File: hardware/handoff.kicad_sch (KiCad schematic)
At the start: 39 parts, among them J1 BAT JST-XH 2p, J2 PAD JST-XH 2p, J3 LED JST-XH 4p / 5mm RGB, J4 EXP 1x10, SW1 SS-12F23G5, U1 Raspberry Pi Pico 2 W, U2 MCP6292-E/MS

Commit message: Draw the SS-12F23G5 footprint and settle C4's pitch
SW1 gets a project footprint in hardware/handoff.pretty taken from the
vendor drawing: three 0.8 x 0.45 mm terminals at 3.0 mm pitch, two mounting
ears 12.9 mm overall, body 8.7 x 5.5 mm standing 3.3 mm behind the pin row.
Loads cleanly and passes DRC on a throwaway board. C4 is a 5 mm can on the
stock 2.5 mm-pitch footprint, per the owner.

Co-Authored-By: Claude Opus 5 <noreply@anthropic.com>
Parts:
- C4: footprint Capacitor_THT:CP_Radial_D5.0mm_P2.00mm -> Capacitor_THT:CP_Radial_D5.0mm_P2.50mm
- SW1: footprint Button_Switch_THT:SW_Slide_SPDT_Angled_CK_OS102011MA1Q -> handoff:SW_Slide_SS-12F23G5

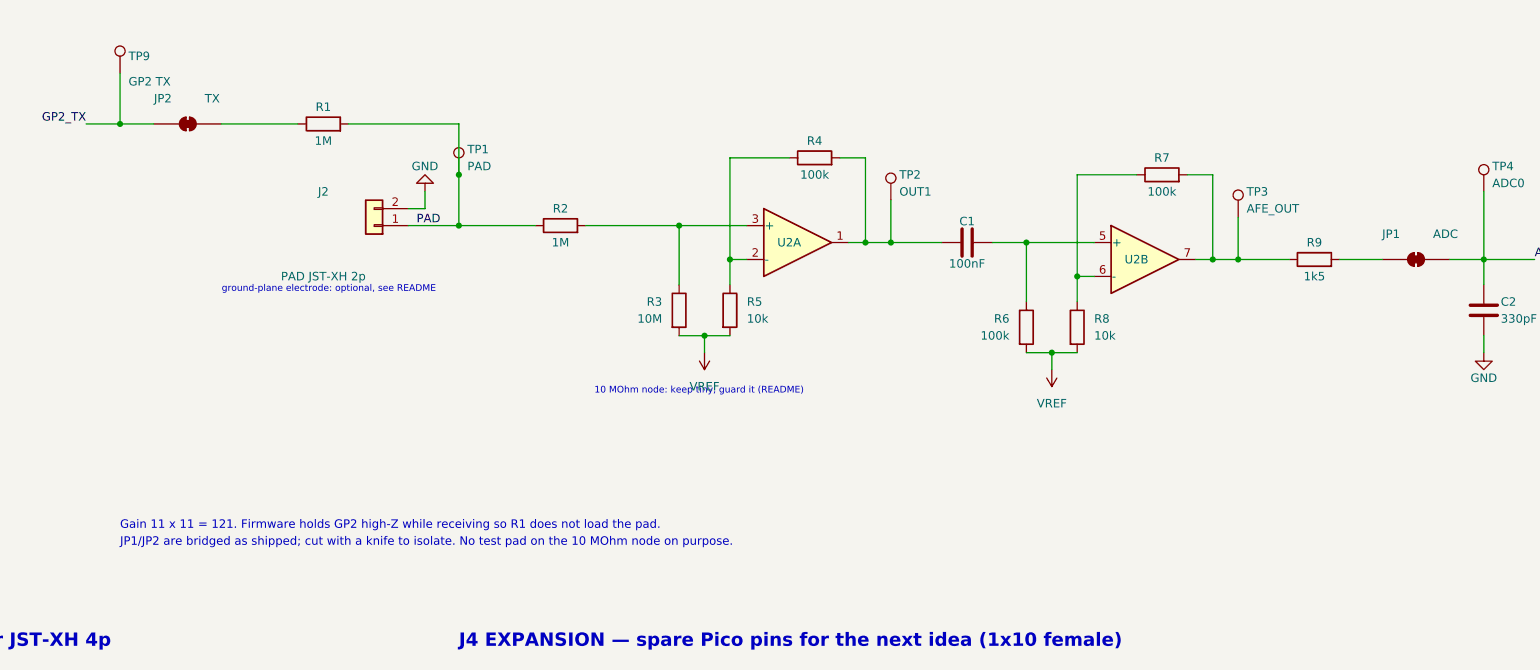
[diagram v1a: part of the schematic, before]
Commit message: Make every solder jumper normally open
Bridge with a blob to connect, wick to isolate; nothing is cut. Owner's
call: a blob is reversible, a knife cut is not. The board is inert as
delivered until JP1 and JP2 are bridged, which the README and the sheet
note now say. The review brief for the next session carries the same rule
into the jumpers it will add.

Co-Authored-By: Claude Opus 5 <noreply@anthropic.com>
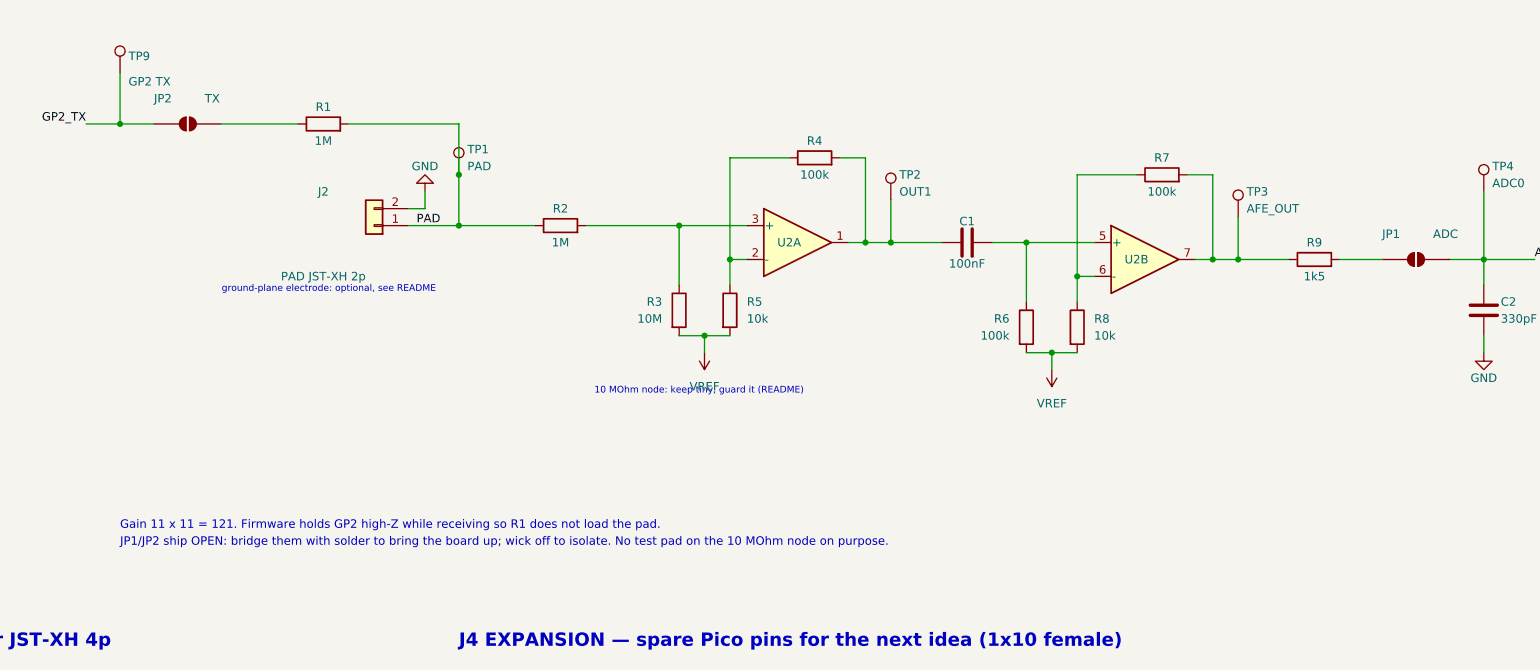
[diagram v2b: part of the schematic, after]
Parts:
- removed JP1: ADC, Jumper:SolderJumper-2_P1.3mm_Bridged_RoundedPad1.0x1.5mm, symbol Jumper:SolderJumper_2_Bridged
- removed JP2: TX, Jumper:SolderJumper-2_P1.3mm_Bridged_RoundedPad1.0x1.5mm, symbol Jumper:SolderJumper_2_Bridged
- added JP1: ADC, Jumper:SolderJumper-2_P1.3mm_Open_RoundedPad1.0x1.5mm, symbol Jumper:SolderJumper_2_Open
- added JP2: TX, Jumper:SolderJumper-2_P1.3mm_Open_RoundedPad1.0x1.5mm, symbol Jumper:SolderJumper_2_Open
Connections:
- net ADC0: now also JP1.2 (B)
- net GP2_TX: now also JP2.1 (A)
- net at R1.1: now also JP2.2 (B)
- net at R9.2: now also JP1.1 (A)
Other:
- note added: "JP1/JP2 ship OPEN: bridge them with solder to bring the board up; wick off to isolate. No test pad on the 10 MOhm node on purpose."
- note removed: "JP1/JP2 are bridged as shipped; cut with a knife to isolate. No test pad on the 10 MOhm node on purpose."

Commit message: Review the schematic before layout, and act on it
Pre-layout review of the untested PCBWay board. Report in hardware/review.md;
the generator is now the schematic's source and proves itself three ways
(ERC, EXPECTED_NETS pin for pin, BOM against the README parts table).

Wiring: all correct. U2 units map to the MCP6292 pinout, all 40 Pico pins
match, D1 and J1 polarity right, chain matches design section 7. 56 footprints
cross-checked pad-for-pad against their symbols with pcbnew. The brief's
"42 pads vs 40 pins" on the Pico footprint was a grep artefact: the two extra
hits are (pads not_allowed)/(pads allowed) inside its antenna keep-out rule.

Circuit, two real problems, both now measurable on the bench:

- GP2 leakage through R3 (10 MOhm) sets stage 1's DC point. 15 nA uses the
  whole headroom; RP2350-E9 can source 46 nA and park OUT1 on the rail. The
  owner's Pico 2 W is an A2, so E9 is live. Firmware must disable GP2's input
  buffer when high-Z; C6 (DNP, across JP2) AC-couples TX as the way out.
- Recovery after the board's own shout is ~3.6 ms on a body against the 1 ms
  budget, plus up to 13 ms through C1/R6 if the OOK-off chips drive GP2 low.
  Mains hum clips stage 2 at 13 mV on the 10 MOhm node.

Recommended but NOT applied, both value-only swaps on existing pads using
parts on hand, so the owner decides at M7: R3 10M -> 1M, C1 100n -> 330p.

Added, pads only unless noted: SW2 + R15 on GP15 (net BTN, the part the owner
chose), H1-H4 M3 mounting holes, J5 charger port in parallel with J1 (needs
one more 2-pin XH header), C5 bulk on U2's rail, C6 (DNP), JP3 3-way stage
select, JP4/JP5/JP6/JP7 in-line isolation, JP8 role strap on GP14, and
TP10-TP13. Every jumper ships open, so each is two nets in the oracle; the
README carries the jumper table and the bring-up order.

Also corrects the SS-12F23G5 footprint, which had the body standing 3.3 mm
behind the pin row with the handle vertical. Measured on the real part: it is
a right-angle switch lying flat on t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
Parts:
- added C5: 10uF 63V, Capacitor_THT:CP_Radial_D5.0mm_P2.50mm, symbol Device:C_Polarized
- added C6: 330pF C0G (DNP), Capacitor_SMD:C_1206_3216Metric_Pad1.33x1.80mm_HandSolder, symbol Device:C
- added H1, H2, H3, H4: M3, MountingHole:MountingHole_3.2mm_M3, symbol Mechanical:MountingHole
- added J5: CHG XH-2, Connector_JST:JST_XH_B2B-XH-A_1x02_P2.50mm_Vertical, symbol Connector_Generic:Conn_01x02
- added JP3: STAGE, Jumper:SolderJumper-3_P1.3mm_Open_RoundedPad1.0x1.5mm, symbol Jumper:SolderJumper_3_Open
- added JP4: U2 VDD, Jumper:SolderJumper-2_P1.3mm_Open_RoundedPad1.0x1.5mm, symbol Jumper:SolderJumper_2_Open
- added JP5: VSYS, Jumper:SolderJumper-2_P1.3mm_Open_RoundedPad1.0x1.5mm, symbol Jumper:SolderJumper_2_Open
- added JP6: VREF, Jumper:SolderJumper-2_P1.3mm_Open_RoundedPad1.0x1.5mm, symbol Jumper:SolderJumper_2_Open
- added JP7: RX, Jumper:SolderJumper-2_P1.3mm_Open_RoundedPad1.0x1.5mm, symbol Jumper:SolderJumper_2_Open
- added JP8: ROLE, Jumper:SolderJumper-2_P1.3mm_Open_RoundedPad1.0x1.5mm, symbol Jumper:SolderJumper_2_Open
- added R15: 10k, Resistor_SMD:R_1206_3216Metric_Pad1.30x1.75mm_HandSolder, symbol Device:R
- added SW2: TACT 6x6, Button_Switch_THT:SW_PUSH_6mm, symbol Switch:SW_Push
- added TP10: BAT+, TestPoint:TestPoint_Pad_D1.5mm, symbol Connector:TestPoint
- added TP11: D1_K, TestPoint:TestPoint_Pad_D1.5mm, symbol Connector:TestPoint
- added TP12: RX_IN, TestPoint:TestPoint_Pad_D1.5mm, symbol Connector:TestPoint
- added TP13: GND, TestPoint:TestPoint_Pad_D1.5mm, symbol Connector:TestPoint
- J1: value BAT JST-XH 2p -> BAT XH-2
- TP6: value 3V3 -> AFE_3V3
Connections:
- net +3V3: now also JP4.1 (A), R15.1; no longer C3.1, R10.1, TP6.1, U2.8 (V+)
- net BAT+: now also J5.2 (Pin_2), TP10.1
- net GND: now also C5.2, J5.1 (Pin_1), JP8.2 (B), SW2.2, TP13.1
- net GP2_TX: now also C6.1
- net PAD: now also JP7.1 (A); no longer R2.1
- net VREF: now also JP6.2 (B); no longer C4.1, R10.2, R11.1
- net VSYS: now also JP5.2 (B); no longer D1.1 (K)
- net at R7.2, TP3.1, U2.7: now also JP3.3 (B); no longer R9.1
- net OUT1: now reaches C1.1, R4.2, TP2.1, U2.1
- net OUT1: now also JP3.1 (A)
- net at JP2.2 (B), R1.1: now also C6.2
- net ROLE: now reaches U1.19 (GPIO14)
- net ROLE: now also JP8.1 (A)
- net BTN: now reaches U1.20 (GPIO15)
- net BTN: now also R15.2, SW2.1
- new net: D1.1 (K), JP5.1 (A), TP11.1
- new net: JP3.2 (C), R9.1
- new net: C4.1, JP6.1 (A), R10.2, R11.1
- new net: JP7.2 (B), R2.1, TP12.1
- new net AFE_3V3: C3.1, C5.1, JP4.2 (B), R10.1, TP6.1, U2.8 (V+)
- no-connect marks 18 -> 16
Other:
- note added: "BUTTON (GP15), ROLE strap (GP14), MOUNTING"
- note added: "Every JP ships OPEN: bridge with solder to bring the board up one stage at a time (README order); wick off to isolate. No test pad on the 10 MOhm node on purpose."
- note added: "Gain 11 x 11 = 121. Firmware holds GP2 high-Z with its input buffer OFF while receiving (RP2350-E9), so R1 does not load or bias the pad."
- note added: "H1-H4: 3.2 mm unplated, one per corner, not tied to GND"
- note added: "JP3: centre -> R9. Blob to pin 3 = stage 2 (x121); move it to pin 1 = stage 1 only (x11) if stage 2 clips. C6 is DNP: fit it instead of bridging JP2 to AC-couple TX."
- note added: "JP5 ships OPEN: bridge it to run from the cell (USB works regardless); open, TP11 -> TP8 is the ammeter position."
- note added: "U2 supply — AFE_3V3 behind JP4 (design §6.4 decoupling + C5 bulk)"
- note added: "VBUS (USB) and VSYS are OR'd inside the Pico; D1 stops VSYS back-feeding the cell and makes a reversed J1 harmless."
- note added: "no debounce cap: debounce in firmware"
- note added: "~0.35 V drop: VSYS 2.6-3.8 V, Pico needs 1.8-5.5 V. J5 is the charger's plug, wired to the cell, NOT a power input."
- note removed: "Gain 11 x 11 = 121. Firmware holds GP2 high-Z while receiving so R1 does not load the pad."
- note removed: "JP1/JP2 ship OPEN: bridge them with solder to bring the board up; wick off to isolate. No test pad on the 10 MOhm node on purpose."
- note removed: "U2 supply (design §6.4 decoupling)"
- note removed: "VBUS (USB) and VSYS are OR'd inside the Pico; D1 stops VSYS back-feeding the cell"
- note removed: "and makes a reversed J1 harmless. ~0.35 V drop: VSYS 2.6-3.8 V, Pico needs 1.8-5.5 V."

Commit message: Bring the schematic up to the floor plan, and settle the two values
The floor plan was settled after the schematic review signed off, and settling
it invalidated decisions the schematic still encoded. Six changes, each with its
EXPECTED_NETS update; the generator still ends ERC 0 violations, 54 nets 0
missing 0 unexpected, README table diff 0.

The RGB LED moves to GP14/13/12 (pins 19/17/16) so J3, hard against the left
edge, faces pins 16-19 straight across with the cathode on pin 18's GND: four
~7 mm traces, no crossings, no pigtail. That displaces ROLE and BTN, which go to
pins 22 and 21 - beside JP8 and SW2. The GP22/GP19 alternative was checked and
rejected: it clears the antenna keep-out but then has to detour around J2 and
the corner boss, which is more copper near the antenna, not less. Both nets are
static DC, which is what the keep-out's "thin escape" allowance is for.

TX moves off GP2 to GP11 (pin 15). GP2 was never special - E9 hits every bank-0
pin equally - and pin 15 is opposite the R2/R3 island, so R1 butts up to it with
a short perpendicular entry instead of a 24 mm run alongside the only critical
node on the board.

J4 stops being a connector. Ten breakout pads E1-E10, each inboard of its own
Pico pin. A 1x10 footprint cannot describe ten scattered positions, and ten
TestPoint symbols make the oracle stricter: ("E7","1") instead of ("J4","7"),
so a mis-numbered header pin can no longer hide in a net of the right size.

D1 takes the 7.62 mm DO-41 footprint - the owner measured the real part against
it, so D1 stays on the little-finger strip and SW2 keeps x = 20. H1-H4 take a
new project footprint at 3.4 mm (ISO 273 medium, for a boss with a brass insert)
carrying the 8 mm keep-out in the footprint, so DRC enforces it wherever the
hole goes.

R3 10M -> 1M and C1 100nF -> 330pF, both the review's own recommendations, now
settled by the owner. Recovery on a body 3.6 ms -> 0.36 ms, inside the §9.7
budget; 40 dB at 50 Hz. Value-only swaps on pads that d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
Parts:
- removed J4: EXP 1x10, Connector_PinSocket_2.54mm:PinSocket_1x10_P2.54mm_Vertical, symbol Connector_Generic:Conn_01x10
- added E1: 3V3 (pin 36), TestPoint:TestPoint_THTPad_D2.0mm_Drill1.0mm, symbol Connector:TestPoint
- added E10: GND (pin 3), TestPoint:TestPoint_THTPad_D2.0mm_Drill1.0mm, symbol Connector:TestPoint
- added E2: RUN (pin 30), TestPoint:TestPoint_THTPad_D2.0mm_Drill1.0mm, symbol Connector:TestPoint
- added E3: GP0 (pin 1), TestPoint:TestPoint_THTPad_D2.0mm_Drill1.0mm, symbol Connector:TestPoint
- added E4: GP1 (pin 2), TestPoint:TestPoint_THTPad_D2.0mm_Drill1.0mm, symbol Connector:TestPoint
- added E5: GP4 (pin 6), TestPoint:TestPoint_THTPad_D2.0mm_Drill1.0mm, symbol Connector:TestPoint
- added E6: GP5 (pin 7), TestPoint:TestPoint_THTPad_D2.0mm_Drill1.0mm, symbol Connector:TestPoint
- added E7: GP20 (pin 26), TestPoint:TestPoint_THTPad_D2.0mm_Drill1.0mm, symbol Connector:TestPoint
- added E8: GP21 (pin 27), TestPoint:TestPoint_THTPad_D2.0mm_Drill1.0mm, symbol Connector:TestPoint
- added E9: GP27 (pin 32), TestPoint:TestPoint_THTPad_D2.0mm_Drill1.0mm, symbol Connector:TestPoint
- C1: value 100nF -> 330pF C0G
- D1: footprint Diode_THT:D_DO-41_SOD81_P10.16mm_Horizontal -> Diode_THT:D_DO-41_SOD81_P7.62mm_Horizontal
- H1, H2, H3, H4: footprint MountingHole:MountingHole_3.2mm_M3 -> handoff:MountingHole_3.4mm_M3_Boss8mm
- R3: value 10M -> 1M
- TP9: value GP2 TX -> GP11 TX
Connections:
- net +3V3: now also E1.1
- net BTN: now also U1.21 (GPIO16); no longer U1.20 (GPIO15)
- net GND: now also E10.1
- net GP0: now also E3.1
- net GP1: now also E4.1
- net GP20: now also E7.1
- net GP21: now also E8.1
- net GP27_ADC1: now also E9.1
- net GP4: now also E5.1
- net GP5: now also E6.1
- net LED_B: now also U1.16 (GPIO12); no longer U1.24 (GPIO18)
- net LED_G: now also U1.17 (GPIO13); no longer U1.22 (GPIO17)
- net LED_R: now also U1.19 (GPIO14); no longer U1.21 (GPIO16)
- net ROLE: now also U1.22 (GPIO17); no longer U1.19 (GPIO14)
- net RUN: now also E2.1
- net GP11_TX: now reaches U1.15 (GPIO11)
- net GP11_TX: now also C6.1, JP2.1 (A), TP9.1
- removed net GP2_TX: C6.1, JP2.1 (A), TP9.1, U1.4 (GPIO2)
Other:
- note added: "BUTTON (GP16), ROLE strap (GP17), MOUNTING"
- note added: "E1-E10 EXPANSION — one breakout pad inboard of its own Pico pin"
- note added: "Gain 11 x 11 = 121. Firmware holds GP11 high-Z with its input buffer OFF while receiving (RP2350-E9), so R1 does not load or bias the pad."
- note added: "H1-H4: 3.4 mm unplated, 8 mm boss keep-out, one per corner, not tied to GND"
- note added: "STATUS LED — RGB common cathode on GP14/13/12, direct-solder or JST-XH 4p"
- note added: "The spare ADC (GP27) is deliberate: a second analogue path is the likeliest hack this board will need."
- note added: "Through-hole, 2.0 mm pad / 1.0 mm drill: a wire solders in. RUN to GND is a reset."
- note removed: "BUTTON (GP15), ROLE strap (GP14), MOUNTING"
- note removed: "Gain 11 x 11 = 121. Firmware holds GP2 high-Z with its input buffer OFF while receiving (RP2350-E9), so R1 does not load or bias the pad."
- note removed: "H1-H4: 3.2 mm unplated, one per corner, not tied to GND"
- note removed: "J4 EXPANSION — spare Pico pins for the next idea (1x10 female)"
- note removed: "STATUS LED — RGB common cathode on GP16/17/18, direct-solder or JST-XH 4p"

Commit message: Fix the Pico's mirrored rows, and SW1's board edge, before placing anything
Two errors in the floor plan, both caught by checking the footprints instead of
the drawing, and both before a single part was placed.

The Pico's two header rows were mirrored. The module sits at 180 degrees -
that is forced, because the USB has to overhang the elbow edge and that is what
puts the antenna keep-out at the hand end. At 180 degrees pins 1-20 land on the
little-finger row and 21-40 on the thumb row, the opposite of what the floor
plan showed. Placed at 180 about (28.9, 60.6), pad 1 reads (28.90, 60.60), pad
21 reads (11.12, 12.34), the antenna zone spans y 10.5-19.5 and the USB zone
y 63.8-83.7. Everything that names a Pico pin and a board position depended on
this being right.

So the LED could not take GP14/13/12: those are little-finger pins, and J3 is on
the thumb wall - which is the wall that faces the sky in a right-hand shake, a
decision taken twice over and not worth undoing to save a pin move. The
requirement never changed: four consecutive pins with a Pico GND in the second
slot, so the LED solders straight in as R, K, G, B. On the thumb row the GND
pins are 23, 28 and 38; pin 23 puts the group at 22-25, which is exactly the
y span the floor plan had already drawn J3 at. Hence GP17 / GND / GP18 / GP19.

With the LED on the thumb row nothing displaces BTN and ROLE, so they stay on
GP15 and GP14 and both sit outside the antenna keep-out anyway. TX on GP11
survives: on the little-finger row it is 4.4 mm from the R2/R3 island at the
same y, still the short perpendicular entry that motivated the move.

SW1's body was drawn 5.5 mm deep, which is its height above the board; in plane
it is 7.1. With the pin row at the drawn x = 8.8 only 2.5 mm of the 5 mm handle
cleared the board edge - not enough to reach through a 1.5 mm wall, and a
contradiction of the footprint's own "board edge" line. The pin row moves to
x = 6.3, which puts the front face on the edge and opens the gap t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
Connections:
- net BTN: now also U1.20 (GPIO15); no longer U1.21 (GPIO16)
- net LED_B: now also U1.25 (GPIO19); no longer U1.16 (GPIO12)
- net LED_G: now also U1.24 (GPIO18); no longer U1.17 (GPIO13)
- net LED_R: now also U1.22 (GPIO17); no longer U1.19 (GPIO14)
- net ROLE: now also U1.19 (GPIO14); no longer U1.22 (GPIO17)
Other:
- note added: "BUTTON (GP15), ROLE strap (GP14), MOUNTING"
- note added: "STATUS LED — RGB common cathode on GP17/18/19, direct-solder or JST-XH 4p"
- note removed: "BUTTON (GP16), ROLE strap (GP17), MOUNTING"
- note removed: "STATUS LED — RGB common cathode on GP14/13/12, direct-solder or JST-XH 4p"
